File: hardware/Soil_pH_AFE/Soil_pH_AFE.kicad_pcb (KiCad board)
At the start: 2 copper layers, 50 x 35 mm, 44 parts, among them J1 INSULATED BNC, J2 HOST / JST PH6, U1 LMP91200, U2 ADS112C04, U3 REF3220 / 2.048V, U4 TPS7A2033 / 3.3V, U5 TPS3839K33 / 2.93V

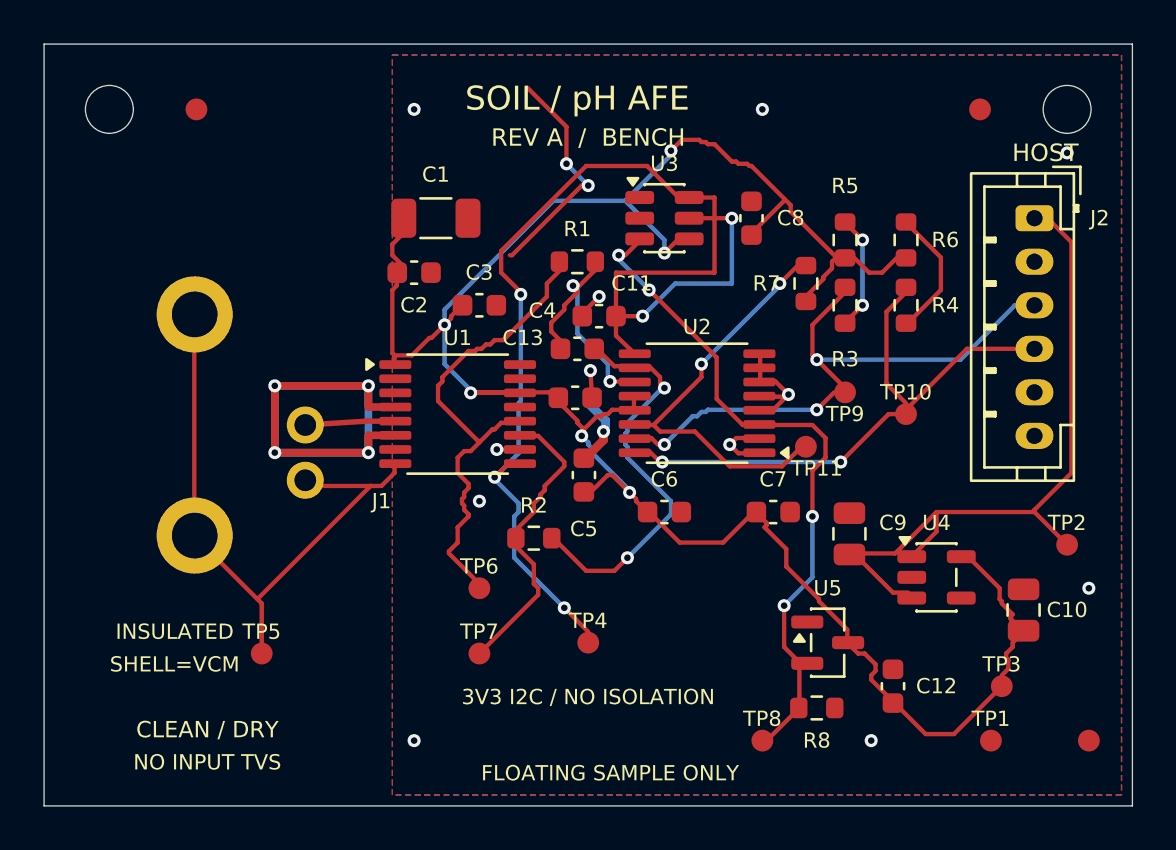
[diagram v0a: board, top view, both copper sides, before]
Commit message: Simplify PCB routes and replace BNC box preview with detailed mesh
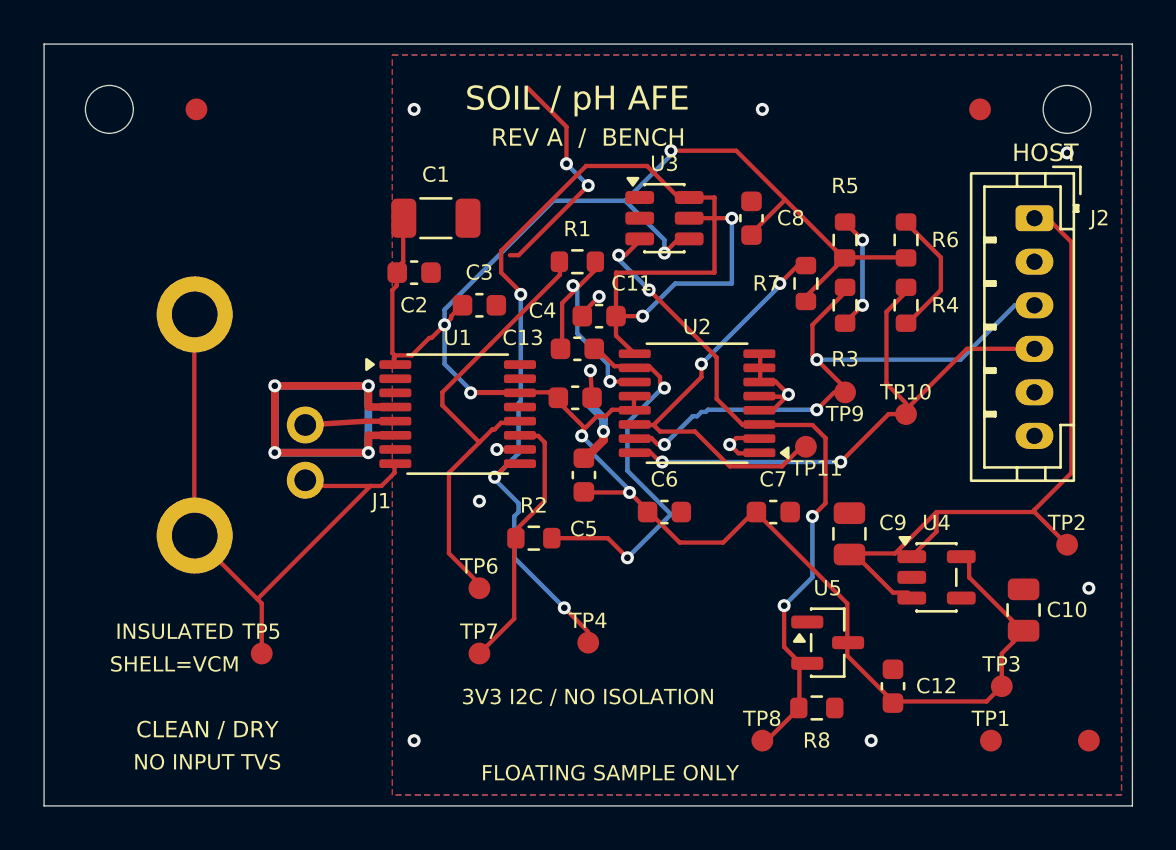
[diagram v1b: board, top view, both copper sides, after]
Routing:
- net +3V3_A: track 99.1 -> 95.3 mm
- net PH_VOCM: track 13.2 -> 11.6 mm
- net PH_VOUT: track 22.3 -> 20.7 mm
- net ADC_N: track 18.2 -> 17.6 mm
